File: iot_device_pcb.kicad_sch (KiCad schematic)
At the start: 8 parts, among them J1 USB_C_Receptacle_USB2.0_16P, U1 ESP32-S3-WROOM-1

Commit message: feat(iot): add USB‑C connector and 3.3V regulator to schematic
Add a USB‑C receptacle and an AMS1117‑3.3 LDO regulator to the iot_device_pcb schematic, along with a small capacitor symbol for decoupling. The autosave backup file was removed as part of the cleanup.
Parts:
- added C3: 10u, Capacitor_SMD:C_0805_2012Metric, symbol Device:C_Small
- added C4: 22u, symbol Device:C_Small
- added U2: AMS1117-3.3, Package_TO_SOT_SMD:SOT-223-3_TabPin2, symbol Regulator_Linear:AMS1117-3.3
- R1, R2, R3: footprint Resistor_SMD:R_0805_2012Metric -> Resistor_SMD:R_0201_0603Metric
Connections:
- net +5V: now also C3.1, U2.3 (VI)
- net GND: now also C3.2, C4.2, U2.1 (GND)
- new net +3.3V: C4.1, U2.2 (VO)
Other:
- note added: "3.3 VOLTAGE REGULATOR"
- moved on the sheet: U1

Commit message: docs(kicad): enrich component properties in iot_device_pcb schematic
Added missing Footprint, Datasheet, Description, Manufacturer, part number, distributor links, and LCSC ID, and set exclude_from_sim to yes for improved component sourcing and simulation filtering.
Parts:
- C4: footprint (none) -> Capacitor_SMD:C_0805_2012Metric; Distributor_link_1 (none) -> https://eu.mouser.com/ProductDetail/Samsung-Electro-Mechani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; Distributor_link_2 (none) -> https://www.digikey.com/en/products/detail/samsung-electro-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; LCSC (none) -> C318688; Manufacturer (none) -> Samsung Electro-Mechanics; Manufacturer_part_number (none) -> CL21A226KPCLRNC
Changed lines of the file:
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@@
 		(at 66.04 100.33 0)
 		(unit 1)
-		(exclude_from_sim no)
+		(exclude_from_sim yes)
 		(in_bom yes)
 		(on_board yes)
@@
 			)
 		)
-		(property "Footprint" ""
+		(property "Footprint" "Capacitor_SMD:C_0805_2012Metric"
 			(at 66.04 100.33 0)
 			(effects
@@
 			)
 		)
-		(property "Datasheet" "~"
+		(property "Datasheet" "https://weblib.samsungsem.com/mlcc/mlcc-ec-data-sheet.do?partNumber=CL21A226KPCLRN"
 			(at 66.04 100.33 0)
 			(effects
@@
 			)
 		)
-		(property "Description" "Unpolarized capacitor, small symbol"
+		(property "Description" "Multilayer Ceramic Capacitors MLCC - SMD/SMT 22uF+/-10% 10V X5R 2 0805"
 			(at 66.04 100.33 0)
 			(effects
+				(font
+					(size 1.27 1.27)
+				)
+				(hide yes)
+			)
+		)
+		(property "Manufacturer" "Samsung Electro-Mechanics"
+			(at 66.04 100.33 0)
+			(effects
+				(font
+					(size 1.27 1.27)
+				)
+				(hide yes)
+			)
+		)
+		(property "Manufacturer_part_number" "CL21A226KPCLRNC"
+			(at 66.04 100.33 0)
+			(effects
+				(font
+					(size 1.27 1.27)
+				)
+				(hide yes)
+			)
+		)
+		(property "Distributor_link_1" "https://eu.mouser.com/ProductDetail/Samsung-Electro-Mechanics/CL21A226KPCLRNC?qs=E6SK%2F3jFIuGJGShlt%252BbGeg%3D%3D"
+			(at 66.04 100.33 0)
+			(effects
+				(font
+					(size 1.27 1.27)
+				)
+				(hide yes)
+			)
+		)
+		(property "Distributor_link_2" "https://www.digikey.com/en/products/detail/samsung-electro-mechanics/CL21A226KPCLRNC/5961270?s=N4IgTCBcDaIMIBkwEYCCYwDYDSAFRASgHJwgC6AvkA"
+			(at 66.04 100.33 0)
+			(effects
+				(font
+					(size 1.27 1.27)
+				)
+				(hide yes)
+			)
+		)
+		(property "LCSC" "C318688"
+			(at 66.04 100.33 0)
+			(effects

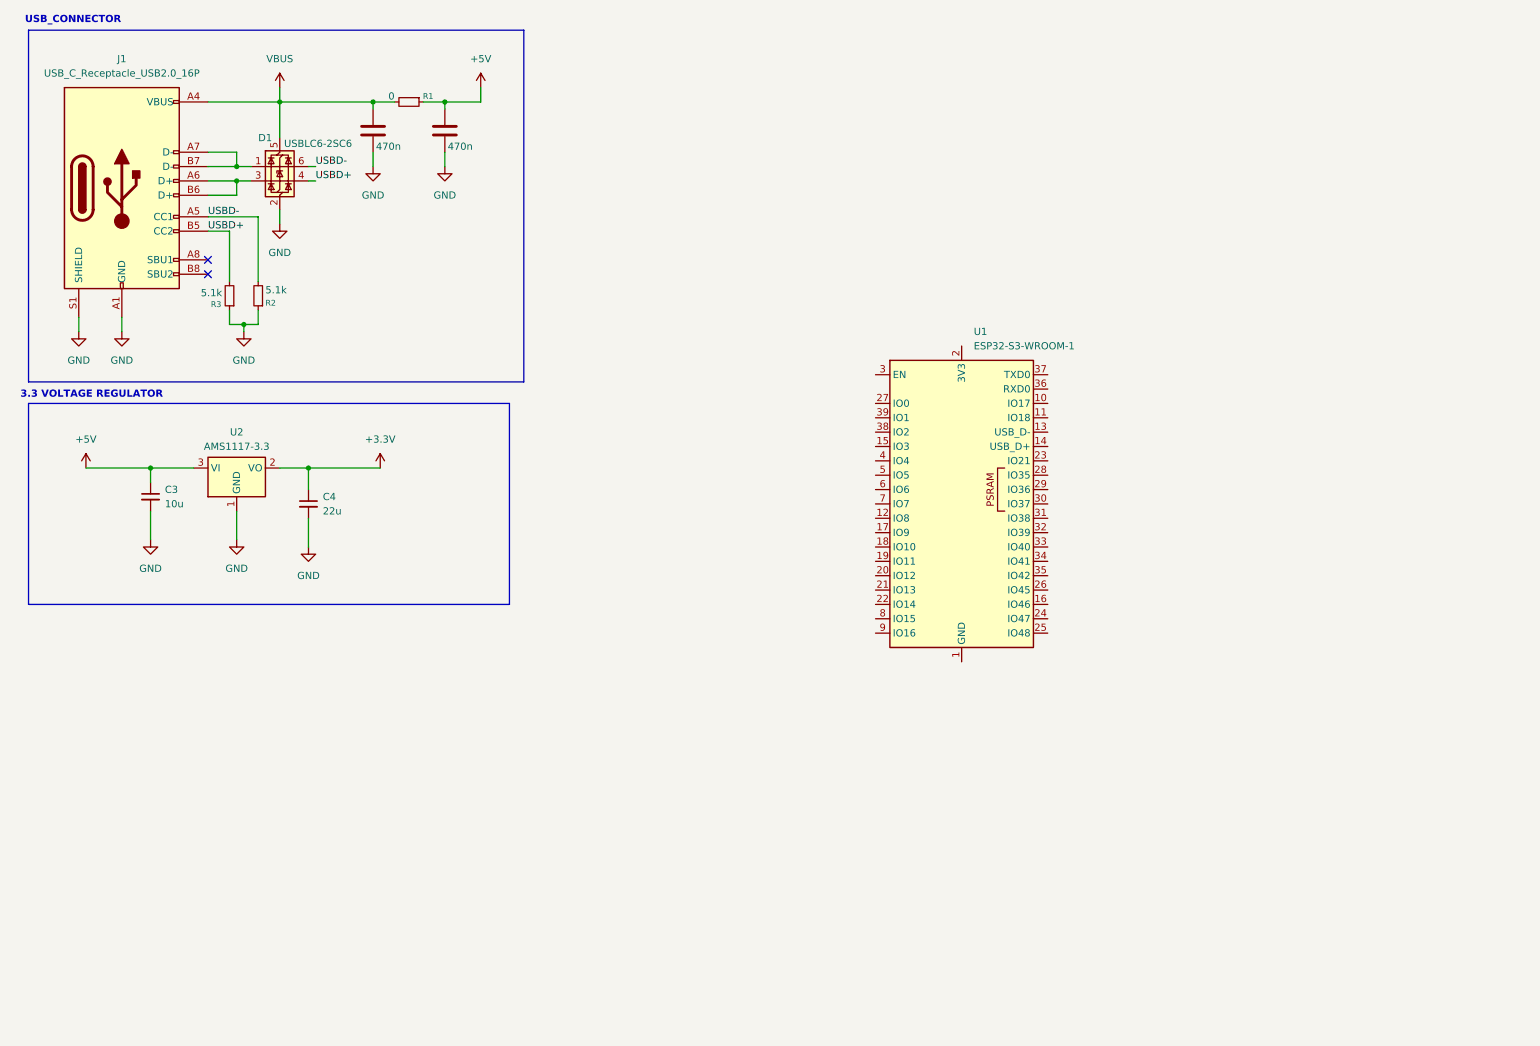
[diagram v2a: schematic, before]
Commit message: refactor(kicad): replace USB connector with LED in iot_device_pcb schematic
Updated iot_device_pcb schematic by swapping USB connector for LED
an LTST-C170KRKT LED component and updated its properties.
Removed the lock flag and adjusted footprint and datasheet.
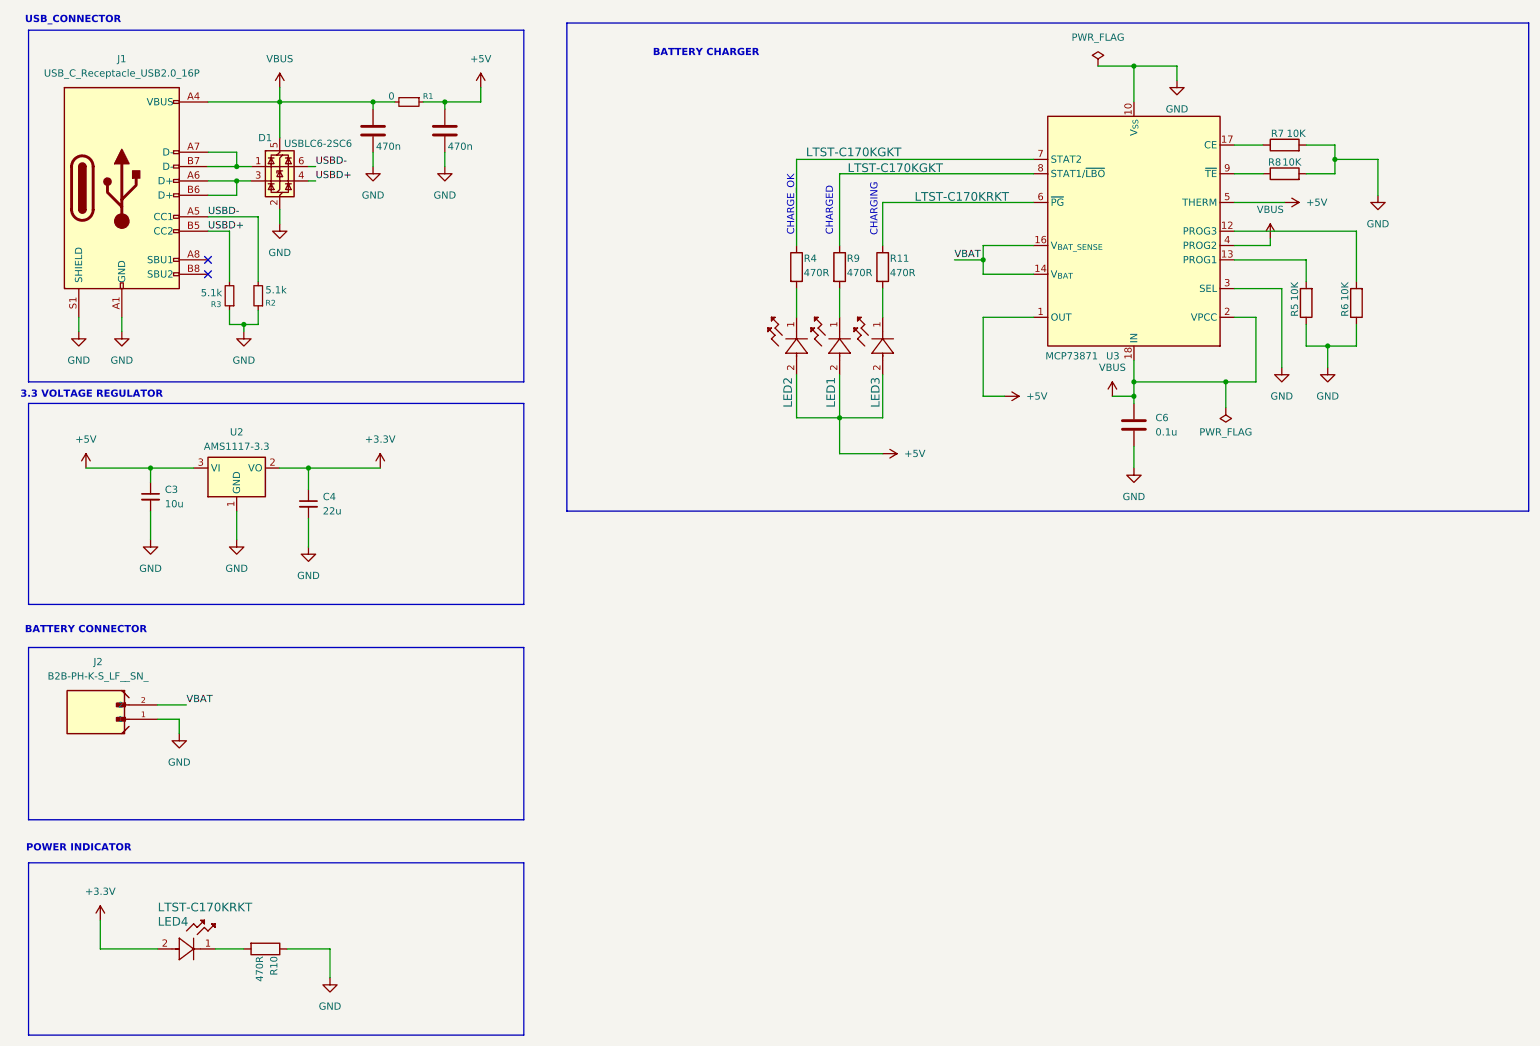
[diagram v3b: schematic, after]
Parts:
- removed U1: ESP32-S3-WROOM-1, RF_Module:ESP32-S3-WROOM-1, symbol RF_Module:ESP32-S3-WROOM-1
- added C6: 0.1u, Capacitor_SMD:C_0805_2012Metric, symbol Device:C
- added J2: B2B-PH-K-S_LF__SN_, FootPrints:JST_B2B-PH-K-S_LF__SN_, symbol B2B-PH-K-S_LF__SN_:B2B-PH-K-S_LF__SN_
- added LED1, LED2: LTST-C170KGKT, LED_SMD:LED_0805_2012Metric, symbol 2025-07-01_05-12-42:LTST-C170KGKT
- added LED3, LED4: LTST-C170KRKT, LED_SMD:LED_0805_2012Metric, symbol 2025-07-01_05-07-46:LTST-C170KRKT
- added R10, R11, R4, R9: 470R, Resistor_SMD:R_0201_0603Metric, symbol Device:R
- added R5, R6, R7, R8: 10K, Resistor_SMD:R_0805_2012Metric, symbol Device:R
- added U3: MCP73871, Package_DFN_QFN:QFN-20-1EP_4x4mm_P0.5mm_EP2.5x2.5mm, symbol Battery_Management:MCP73871
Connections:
- net +3.3V: now also LED4.2
- net +5V: now also LED1.2, LED2.2, LED3.2, U3.1 (OUT), U3.20 (OUT), U3.5 (THERM)
- net GND: now also C6.2, J2.1, R10.1, R5.1, R6.1, R7.2, R8.2, U3.10 (V_{SS}), U3.11 (V_{SS}), U3.21 (V_{SS}), U3.3 (SEL)
- net VBUS: now also C6.1, U3.18 (IN), U3.19 (IN), U3.2 (VPCC), U3.4 (PROG2)
- new net: R7.1, U3.17 (CE)
- new net: LED1.1, R9.2
- new net: R6.2, U3.12 (PROG3)
- new net: R5.2, U3.13 (PROG1)
- new net: R11.1, U3.6 (~{PG})
- new net: R4.1, U3.7 (STAT2)
- new net: R9.1, U3.8 (STAT1/~{LBO})
- new net: R8.1, U3.9 (~{TE})
- new net: LED2.1, R4.2
- new net: LED4.1, R10.2
- new net: LED3.1, R11.2
- new net VBAT: J2.2, U3.14 (V_{BAT}), U3.15 (V_{BAT}), U3.16 (V_{BAT_SENSE})
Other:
- note added: "BATTERY CHARGER"
- note added: "BATTERY CONNECTOR"
- note added: "CHARGED"
- note added: "CHARGE_OK"
- note added: "CHARGING"
- note added: "POWER INDICATOR"

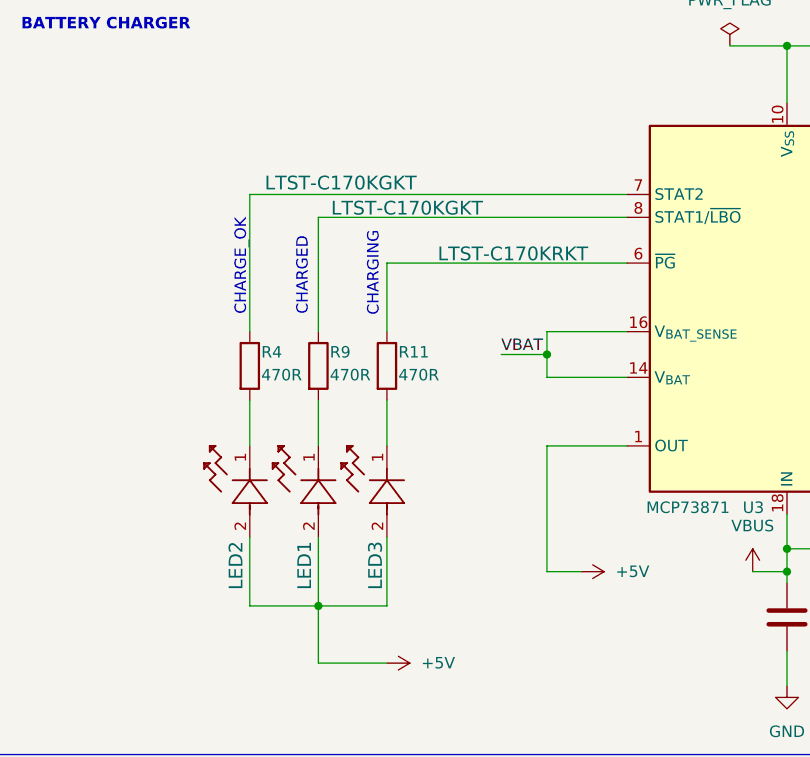
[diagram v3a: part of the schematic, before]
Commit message: refactor(kicad): remove unused LTST-C170KGKT symbol
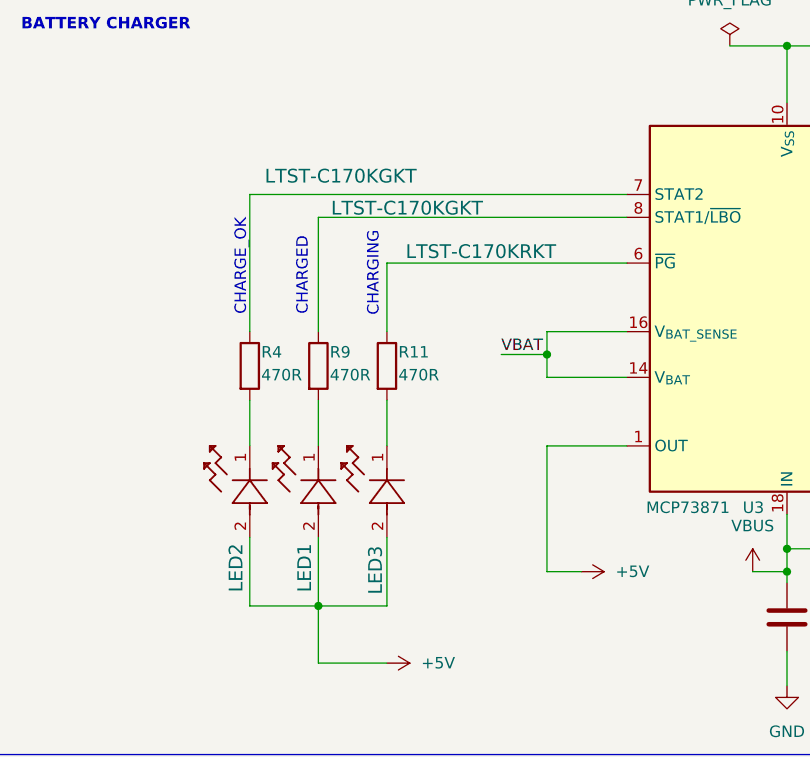
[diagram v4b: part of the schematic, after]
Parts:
- removed LED1, LED2: LTST-C170KGKT, LED_SMD:LED_0805_2012Metric, symbol 2025-07-01_05-12-42:LTST-C170KGKT
- added LED1, LED2: LTST-C170KGKT, LED_SMD:LED_0805_2012Metric, symbol 2025-07-01_05-07-46:LTST-C170KRKT
- LED3, LED4: Distributor_link_1 (none) -> https://eu.mouser.com/ProductDetail/LITEON/LTST-C170KGKT?qs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; Distributor_link_2 (none) -> https://www.digikey.com/en/products/detail/liteon/LTST-C170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; LCSC (none) -> C94868; Manufacturer (none) -> LITEON; Manufacturer_part_number (none) -> LTST-C170KRKT
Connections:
- net +5V: now also LED1.2, LED2.2
- net at R9.2: now also LED1.1
- net at R4.2: now also LED2.1

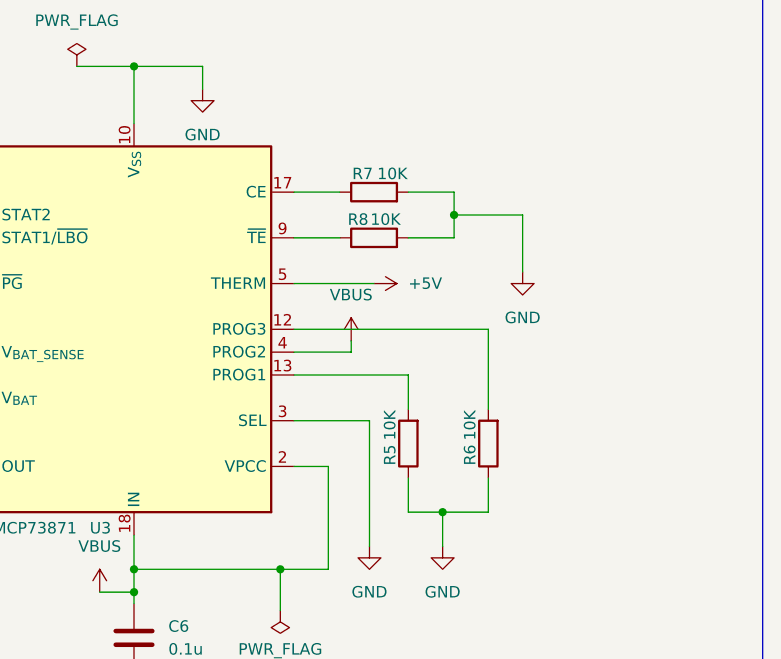
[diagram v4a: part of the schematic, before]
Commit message: refactor(kicad): enrich component metadata for R7 resistor and MCP73871
Add detailed datasheet links, comprehensive descriptions, manufacturer information, and distributor URLs for the R7 resistor and MCP73871 battery charger in the schematic. These updates improve traceability and reduce lookup time for parts.
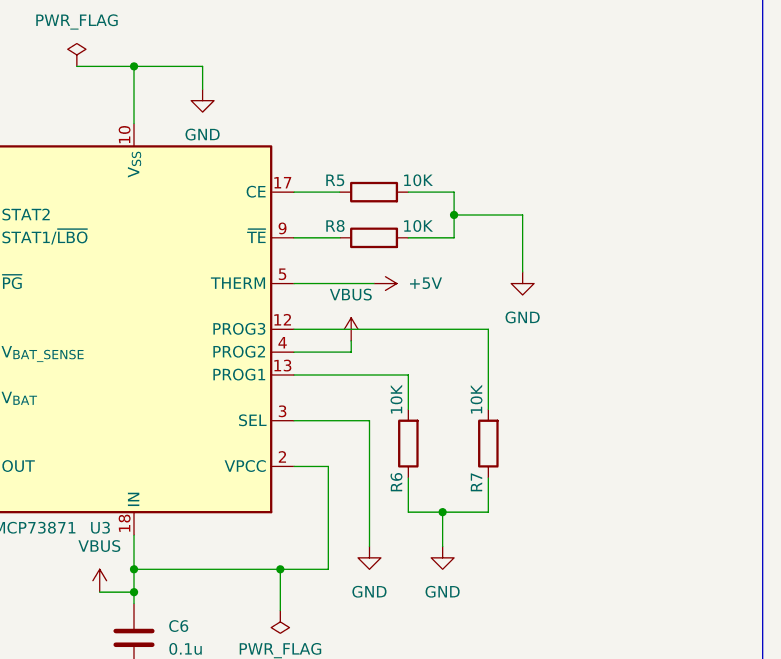
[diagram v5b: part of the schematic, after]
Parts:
- R5, R6, R7, R8: Distributor_link_1 (none) -> https://eu.mouser.com/ProductDetail/Vishay/CRCW121810K0FKEK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; Distributor_link_2 (none) -> https://www.digikey.com/en/products/detail/vishay-dale/CRCW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; LCSC (none) -> C2144629; Manufacturer (none) -> CRCW121810K0FKEK; Manufacturer_part_number (none) -> Vishay
- U3: Distributor_link_1 (none) -> https://eu.mouser.com/ProductDetail/Microchip-Technology/MC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; Distributor_link_2 (none) -> https://www.digikey.com/en/products/detail/microchip-techno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; LCSC (none) -> C637761; Manufacturer (none) -> Microchip Technology; Manufacturer_part_number (none) -> MCP73871-4CAI/ML
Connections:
- net GND: now also R5.2, R7.1; no longer R5.1, R7.2
- net at U3.17 (CE): now also R5.1; no longer R7.1
- net at U3.12 (PROG3): now also R7.2; no longer R6.2
- net at U3.13 (PROG1): now also R6.2; no longer R5.2
